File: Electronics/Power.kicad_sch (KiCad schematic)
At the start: 53 parts, among them IC1 TPS65251-1RHAR

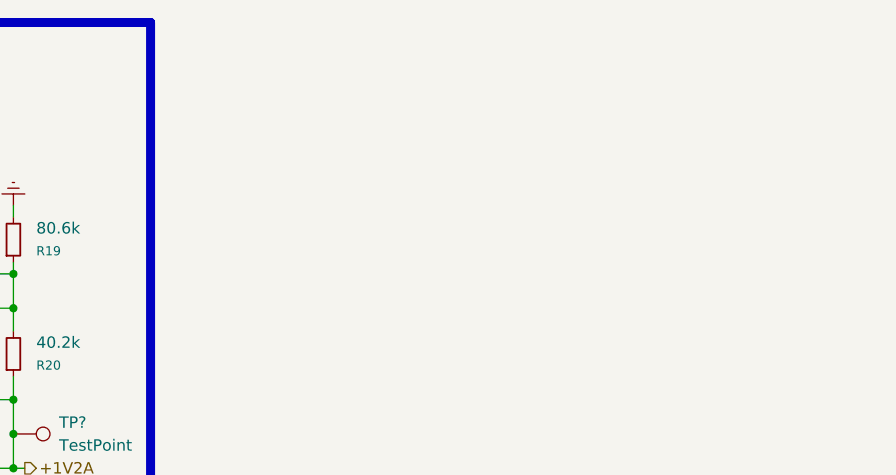
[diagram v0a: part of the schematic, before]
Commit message: RP2040 Added, Files Structure Changed
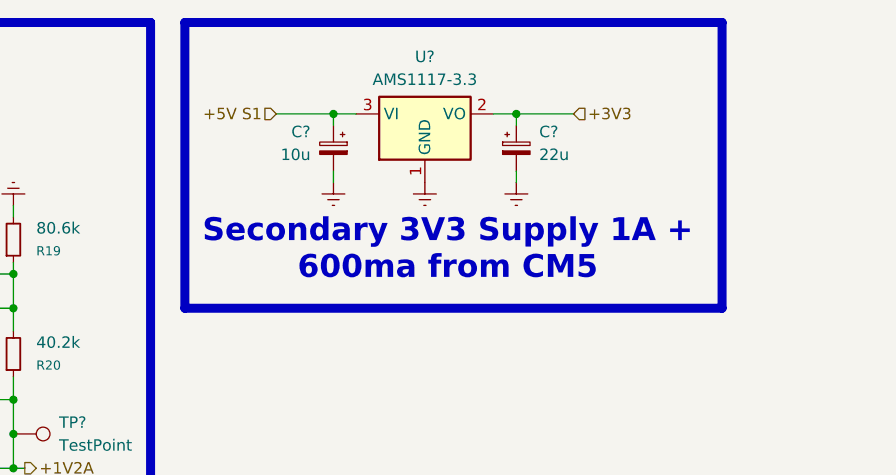
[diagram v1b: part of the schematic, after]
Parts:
- added C?: 10u, symbol Device:C_Polarized_Small
- added C?: 22u, symbol Device:C_Polarized_Small
- added U?: AMS1117-3.3, Package_TO_SOT_SMD:SOT-223-3_TabPin2, symbol Regulator_Linear:AMS1117-3.3
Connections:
- net +5V S1: now also C?.1, U?.3 (VI)
- new net +3V3: C?.1, U?.2 (VO)

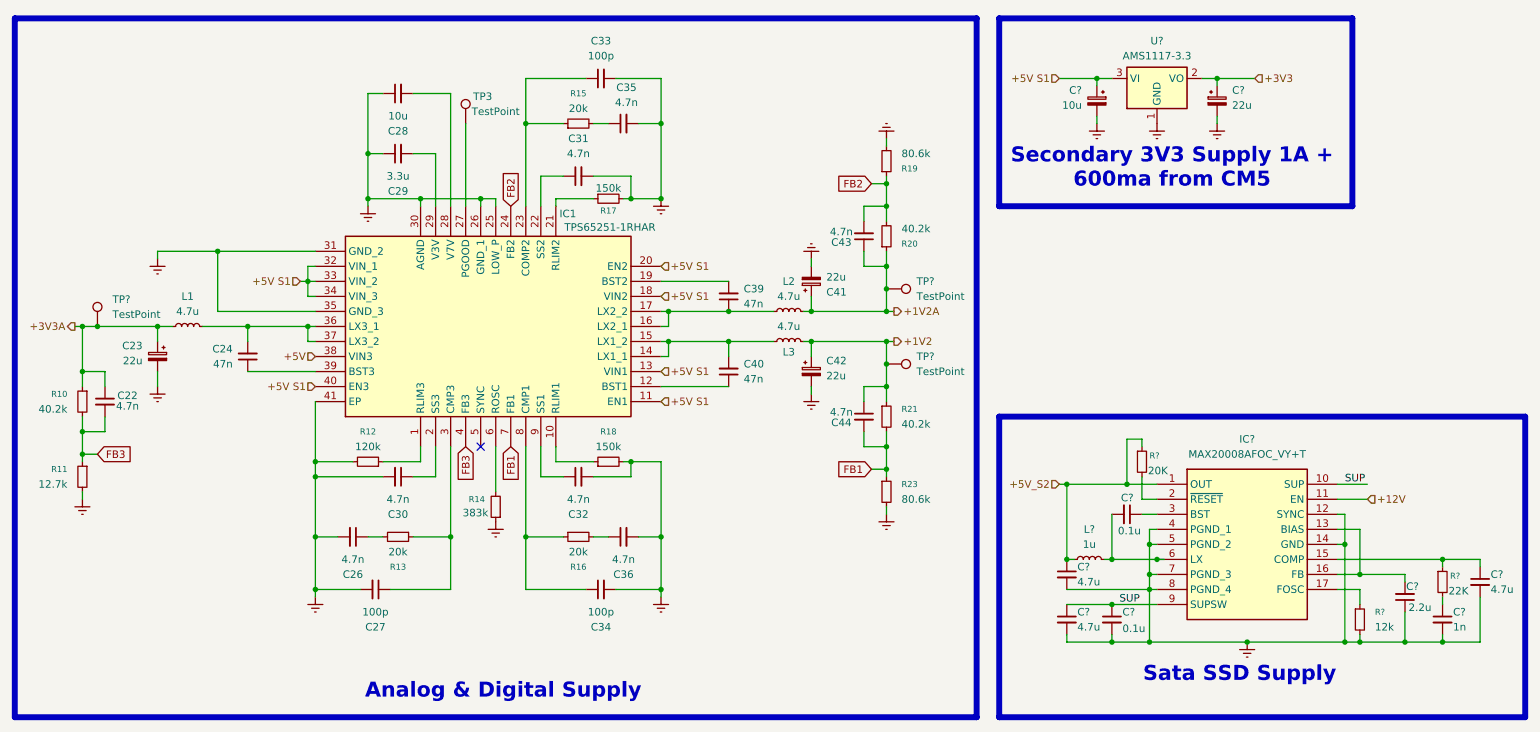
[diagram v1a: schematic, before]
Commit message: Starting the Sheet connections
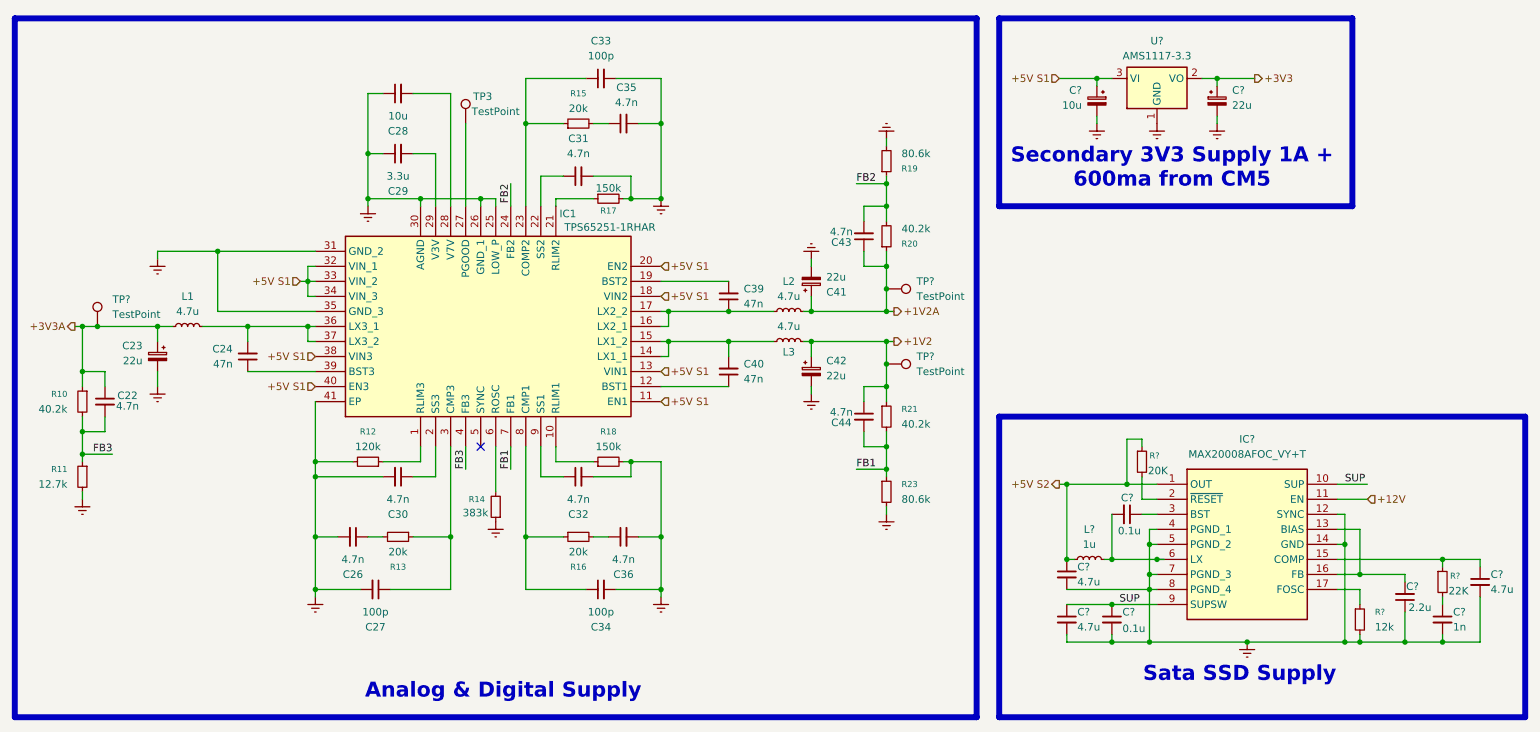
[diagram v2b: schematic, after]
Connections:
- net +5V is gone; now on net +5V S1: IC1.38 (VIN3)
- net +5V_S2 renamed +5V S2
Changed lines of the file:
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@@
 	(wire
 		(pts
-			(xy 162.56 44.45) (xy 165.1 44.45)
+			(xy 160.02 44.45) (xy 165.1 44.45)
 		)
 		(stroke
@@
 	(wire
 		(pts
-			(xy 162.56 92.71) (xy 165.1 92.71)
+			(xy 160.02 92.71) (xy 165.1 92.71)
 		)
 		(stroke
@@
 	(wire
 		(pts
+			(xy 101.6 44.45) (xy 101.6 48.26)
+		)
+		(stroke
+			(width 0)
+			(type default)
+		)
+	)
+	(wire
+		(pts
 			(xy 210.82 95.25) (xy 205.74 95.25)
 		)
@@
 	(wire
 		(pts
+			(xy 101.6 92.71) (xy 101.6 88.9)
+		)
+		(stroke
+			(width 0)
+			(type default)
+		)
+	)
+	(wire
+		(pts
 			(xy 161.29 88.9) (xy 165.1 88.9)
 		)
@@
 	(wire
 		(pts
+			(xy 93.98 92.71) (xy 93.98 88.9)
+		)
+		(stroke
+			(width 0)
+			(type default)
+		)
+	)
+	(wire
+		(pts
 			(xy 161.29 48.26) (xy 165.1 48.26)
 		)
@@
 	(wire
 		(pts
-			(xy 31.75 90.17) (xy 29.21 90.17)
+			(xy 34.29 90.17) (xy 29.21 90.17)
 		)
 		(stroke
@@
 		)
 	)
+	(label "FB2"
+		(at 160.02 44.45 0)
+		(effects
+			(font
+				(size 1.27 1.27)
+			)
+			(justify left bottom)
+		)
+	)
+	(label "FB2"
+		(at 101.6 44.45 270)
+		(effects
+			(font
+				(size 1.27 1.27)
+			)
+			(justify right bottom)
+		)
+	)
+	(label "FB1"
+		(at 160.02 92.71 0)
+		(effects
+			(font
+				(size 1.27 1.27)
+			)
+			(justify left bottom)
+		)
+	)
+	(label "FB3"
+		(at 34.29 90.17 180)
+		(effects
+			(font
+				(size 1.27 1.27)
+			)
+			(justify right bottom)
+		)
+	)
+	(label "FB3"
+		(at 93.98 92.71 90)
+		(effects
+			(font
+				(size 1.27 1.27)
+			)
+			(justify left bottom)
+		)
+	)
+	(label "FB1"
+		(at 101.6 92.71 90)
+		(effects
+			(font
+				(size 1.27 1.27)
+			)
+			(justify left bottom)
+		)
+	)
 	(label "SUP"
 		(at 242.57 95.25 0)
@@
 			)
 			(justify left bottom)
-		)
-	)
-	(global_label "FB3"
-		(shape input)
-		(at 31.75 90.17 0)
-		(fields_autoplaced yes)
-		(effects
-			(font
-				(size 1.27 1.27)
-			)
-			(justify left)
-		)
-		(property "Intersheetrefs" "${INTERSHEET_REFS}"
-			(at 38.3033 90.17 0)
-			(effects
-				(font
-					(size 1.27 1.27)
-				)
-				(justify left)
-				(hide yes)
-			)
-		)
-	)
-	(global_label "FB2"
-		(shape input)
-		(at 162.56 44.45 180)
-		(fields_autoplaced yes)
-		(effects
-			(font
-				(size 1.27 1.27)
-			)
-			(justify right)
-		)
-		(property "Intersheetrefs" "${INTERSHEET_REFS}"
-			(at 156.0067 44.45 0)
-			(effects
-				(font
-					(size 1.27 1.27)
-				)
-				(justify right)
-				(hide yes)
-			)
-		)
-	)
-	(global_label "FB1"
-		(shape input)
-		(at 162.56 92.71 180)
-		(fields_autoplaced yes)
-		(effects
-			(font
-				(size 1.27 1.27)
-			)
-			(justify right)
-		)
-		(property "Intersheetrefs" "${INTERSHEET_REFS}"
-			(at 156.0067 92.71 0)
-			(effects
-				(font
-					(size 1.27 1.27)
-				)
-				(justify right)
-				(hide yes)
-			)
-		)
-	)
-	(global_label "FB1"
-		(shape input)
-		(at 101.6 88.9 270)
-		(fields_autoplaced yes)
-		(effects
-			(font
-				(size 1.27 1.27)
-			)
-			(justify right)
-		)
-		(property "Intersheetrefs" "${INTERSHEET_REFS}"
-			(at 101.6 95.4533 90)
-			(effects
-				(font
-					(size 1.27 1.27)
-				)
-				(justify right)
-				(hide yes)
-			)
-		)
-	)
-	(global_label "FB3"
-		(shape input)
-		(at 93.98 88.9 270)
-		(fields_autoplaced yes)
-		(effects
-			(font
-				(size 1.27 1.27)
-			)
-			(justify right)
-		)
-		(property "Intersheetrefs" "${INTERSHEET_REFS}"
-			(at 93.98 95.4533 90)
-			(effects
-				(font
-					(size 1.27 1.27)
-				)
-				(justify right)
-				(hide yes)
-			)
-		)
-	)
-	(global_label "FB2"
-		(shape input)
-		(at 101.6 48.26 90)
-		(fields_autoplaced yes)
-		(effects
-			(font
-				(size 1.27 1.27)
-			)
-			(justify left)
-		)
-		(property "Intersheetrefs" "${INTERSHEET_REFS}"
-			(at 101.6 41.7067 90)
-			(effects
-				(font
-					(size 1.27 1.27)
-				)
-				(justify left)
-				(hide yes)
-			)
 		)
 	)
@@
 		)
 	)
-	(hierarchical_label "+5V_S2"
-		(shape input)
+	(hierarchical_label "+5V S2"
+		(shape output)
 		(at 194.31 95.25 180)
 		(effects
@@
 	)
 	(hierarchical_label "+3V3"
-		(shape input)
+		(shape output)
 		(at 227.33 26.67 0)
 		(effects
@@
 		)
 	)
-	(hierarchical_label "+5V"
+	(hierarchical_label "+5V S1"
 		(shape input)
 		(at 68.58 73.66 180)

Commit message: Footprints Selected
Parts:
- added C46: 100u, EEE_FTH101XAP:CAP_EEEFTH101XAP, symbol Device:C_Polarized_Small
- added C48: 0.1u, Capacitor_SMD:C_0603_1608Metric, symbol Device:C_Small
- added C50: 4.7u, Capacitor_SMD:C_0603_1608Metric, symbol Device:C_Small
- added D10, D11, D7, D8, D9: LED Green, LED_SMD:LED_0603_1608Metric, symbol Device:LED
- added R26, R27, R28, R29, R30: 1K, Resistor_SMD:R_0603_1608Metric, symbol Device:R_Small
- C20: renamed from C22; footprint (none) -> Capacitor_SMD:C_0603_1608Metric
- C21: renamed from C23; footprint (none) -> EEEFK1A220AR:CAP_EEEFK1A220AR
- C22: renamed from C24; footprint (none) -> Capacitor_SMD:C_0603_1608Metric
- C23: renamed from C26; footprint (none) -> Capacitor_SMD:C_0603_1608Metric
- C24: renamed from C27; footprint (none) -> Capacitor_SMD:C_0603_1608Metric
- C25: renamed from C28; footprint (none) -> Capacitor_SMD:C_0603_1608Metric
- C26: renamed from C29; footprint (none) -> Capacitor_SMD:C_0603_1608Metric
- C27: renamed from C30; footprint (none) -> Capacitor_SMD:C_0603_1608Metric
- C28: renamed from C31; footprint (none) -> Capacitor_SMD:C_0603_1608Metric
- C29: renamed from C32; footprint (none) -> Capacitor_SMD:C_0603_1608Metric
- C30: renamed from C33; footprint (none) -> Capacitor_SMD:C_0603_1608Metric
- C31: renamed from C34; footprint (none) -> Capacitor_SMD:C_0603_1608Metric
- C32: renamed from C35; footprint (none) -> Capacitor_SMD:C_0603_1608Metric
- C33: renamed from C36; footprint (none) -> Capacitor_SMD:C_0603_1608Metric
- C34: renamed from C39; footprint (none) -> Capacitor_SMD:C_0603_1608Metric
- C35: renamed from C40; footprint (none) -> Capacitor_SMD:C_0603_1608Metric
- C36: renamed from C41; footprint (none) -> EEEFK1A220AR:CAP_EEEFK1A220AR
- C37: renamed from C42; footprint (none) -> EEEFK1A220AR:CAP_EEEFK1A220AR
- C38: renamed from C43; footprint (none) -> Capacitor_SMD:C_0603_1608Metric
- C39: renamed from C44; footprint (none) -> Capacitor_SMD:C_0603_1608Metric
- C40, C41, C43, C44, C47, C49, C51: renamed from C?; footprint (none) -> Capacitor_SMD:C_0603_1608Metric
- C42: renamed from C?; footprint (none) -> EEEFK1H100UR:CAP_EEEFK1H100UR
- C45: renamed from C?; footprint (none) -> EEEFK1A220AR:CAP_EEEFK1A220AR
- IC1: footprint QFN50P600X600X100-41N-D -> TPS65251-1RHAR:QFN50P600X600X100-41N-D
- IC2: renamed from IC?; footprint MAX20008AFOCVYT -> MAX20008AFOC_VY+T:MAX20008AFOCVYT
- L1, L2, L3: footprint (none) -> SRN5040-4R7M:INDPM5050X400N
- L4: renamed from L?; footprint (none) -> SRN5040TA-1R0M:SRN5040TA1R0M
- R13: renamed from R10; footprint (none) -> Resistor_SMD:R_0603_1608Metric
- R14: renamed from R11; footprint (none) -> Resistor_SMD:R_0603_1608Metric
- R15: renamed from R12; footprint (none) -> Resistor_SMD:R_0603_1608Metric
- R16: renamed from R13; footprint (none) -> Resistor_SMD:R_0603_1608Metric
- R17: renamed from R14; footprint (none) -> Resistor_SMD:R_0603_1608Metric
- R18: renamed from R15; footprint (none) -> Resistor_SMD:R_0603_1608Metric
- R19: renamed from R16; footprint (none) -> Resistor_SMD:R_0603_1608Metric
- R20: renamed from R17; footprint (none) -> Resistor_SMD:R_0603_1608Metric
- R21: renamed from R18; footprint (none) -> Resistor_SMD:R_0603_1608Metric
- R22: renamed from R19; footprint (none) -> Resistor_SMD:R_0603_1608Metric
- R23: renamed from R20; footprint (none) -> Resistor_SMD:R_0603_1608Metric
- R24: renamed from R21; footprint (none) -> Resistor_SMD:R_0603_1608Metric
- R25: renamed from R23; footprint (none) -> Resistor_SMD:R_0603_1608Metric
- R31, R32, R33: renamed from R?; footprint (none) -> Resistor_SMD:R_0603_1608Metric
- TP6, TP8, TP9: renamed from TP?; footprint (none) -> TestPoint:TestPoint_Pad_1.0x1.0mm
- TP7: renamed from TP3; footprint (none) -> TestPoint:TestPoint_Pad_1.0x1.0mm
- gave numbers to parts that had none: 1
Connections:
- net +12V: now also C46.1, C48.1, C50.1
- net +1V2: now also R27.2
- net +1V2A: now also R26.2
- net +3V3: now also R28.2
- net +3V3A: now also R29.2
- net +5V S2: now also R30.2
- new net: D10.1 (K), D11.1 (K), D7.1 (K), D8.1 (K), D9.1 (K)
- new net: D8.2 (A), R27.1
- new net: D7.2 (A), R26.1
- new net: D10.2 (A), R29.1
- new net: D9.2 (A), R28.1
- new net: C46.2, C48.2, C50.2
- new net: D11.2 (A), R30.1

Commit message: Footprints selected, Hiracicle connections created, Pcb next
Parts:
- removed D7, D8: LED Green, LED_SMD:LED_0603_1608Metric, symbol Device:LED
- removed R26, R27: 1K, Resistor_SMD:R_0603_1608Metric, symbol Device:R_Small
- added TP11, TP6: TestPoint, TestPoint:TestPoint_Pad_1.0x1.0mm, symbol Connector:TestPoint
- C20: renamed from C30; footprint Capacitor_SMD:C_0603_1608Metric -> Capacitor_SMD:C_0402_1005Metric
- C21: renamed from C25; footprint Capacitor_SMD:C_0603_1608Metric -> Capacitor_SMD:C_0805_2012Metric
- C24: renamed from C32; value 4.7n -> 4n7; footprint Capacitor_SMD:C_0603_1608Metric -> Capacitor_SMD:C_0402_1005Metric
- C25: renamed from C26; value 3.3u -> 3u3; footprint Capacitor_SMD:C_0603_1608Metric -> Capacitor_SMD:C_0805_2012Metric
- C26: renamed from C28; value 4.7n -> 4n7; footprint Capacitor_SMD:C_0603_1608Metric -> Capacitor_SMD:C_0402_1005Metric
- C27: renamed from C38; value 4.7n -> 4n7; footprint Capacitor_SMD:C_0603_1608Metric -> Capacitor_SMD:C_0402_1005Metric
- C29: renamed from C34; footprint Capacitor_SMD:C_0603_1608Metric -> Capacitor_SMD:C_0402_1005Metric
- C31: renamed from C22; footprint Capacitor_SMD:C_0603_1608Metric -> Capacitor_SMD:C_0402_1005Metric
- C32: renamed from C35; footprint Capacitor_SMD:C_0603_1608Metric -> Capacitor_SMD:C_0402_1005Metric
- C34: renamed from C20; value 4.7n -> 4n7; footprint Capacitor_SMD:C_0603_1608Metric -> Capacitor_SMD:C_0402_1005Metric
- C35: renamed from C39; value 4.7n -> 4n7; footprint Capacitor_SMD:C_0603_1608Metric -> Capacitor_SMD:C_0402_1005Metric
- C36: renamed from C27; value 4.7n -> 4n7; footprint Capacitor_SMD:C_0603_1608Metric -> Capacitor_SMD:C_0402_1005Metric
- C37: renamed from C29; value 4.7n -> 4n7; footprint Capacitor_SMD:C_0603_1608Metric -> Capacitor_SMD:C_0402_1005Metric
- C38: renamed from C44; value 0.1u -> 100n
- C40: renamed from C48; value 0.1u -> 100n; footprint Capacitor_SMD:C_0603_1608Metric -> Capacitor_SMD:C_0402_1005Metric
- C41: renamed from C50; value 4.7u -> 4u7; footprint Capacitor_SMD:C_0603_1608Metric -> Capacitor_SMD:C_0805_2012Metric
- C42: renamed from C23; value 4.7n -> 4n7; footprint Capacitor_SMD:C_0603_1608Metric -> Capacitor_SMD:C_0402_1005Metric
- C43: renamed from C33; value 4.7n -> 4n7; footprint Capacitor_SMD:C_0603_1608Metric -> Capacitor_SMD:C_0402_1005Metric
- C44: renamed from C40; value 4.7u -> 4u7; footprint Capacitor_SMD:C_0603_1608Metric -> Capacitor_SMD:C_0805_2012Metric
- C45: renamed from C51; value 4.7u -> 4u7; footprint Capacitor_SMD:C_0603_1608Metric -> Capacitor_SMD:C_0805_2012Metric
- C46: renamed from C24; footprint Capacitor_SMD:C_0603_1608Metric -> Capacitor_SMD:C_0402_1005Metric
- C47: renamed from C31; footprint Capacitor_SMD:C_0603_1608Metric -> Capacitor_SMD:C_0402_1005Metric
- C48: renamed from C47; value 2.2u -> 2u2
- C49: renamed from C41; value 4.7u -> 4u7; footprint Capacitor_SMD:C_0603_1608Metric -> Capacitor_SMD:C_0805_2012Metric
- C50: renamed from C43; value 0.1u -> 100n
- C51: renamed from C49; footprint Capacitor_SMD:C_0603_1608Metric -> Capacitor_SMD:C_0402_1005Metric
- L1: renamed from L2; value 4.7u -> 4u7
- L2: renamed from L1; value 4.7u -> 4u7
- L3: value 4.7u -> 4u7
- R14: renamed from R22; value 80.6k -> 80K6
- R16: renamed from R23; value 40.2k -> 40K2
- R17: renamed from R28; value 1K -> 270
- R18: renamed from R29; value 1K -> 270
- R20: renamed from R13; value 40.2k -> 40K2
- R21: renamed from R24; value 40.2k -> 40K2
- R25: renamed from R14; value 12.7k -> 12K7
- R26: renamed from R25; value 80.6k -> 80K6
- TP10: renamed from TP9; now not fitted; now left out of the parts list
- TP8: now not fitted; now left out of the parts list
- TP9: renamed from TP6; now not fitted; now left out of the parts list
- renumbered C42 to C22, C45 to C23, C36 to C28, C21 to C30, C37 to C33, C46 to C39, D9 to D7, D10 to D8, D11 to D9, R18 to R13, R20 to R15, R30 to R19, R15 to R22, R21 to R23, R31 to R24, R17 to R27, R16 to R28, R19 to R29, R33 to R30, R32 to R31
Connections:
- net +3V3: now also TP6.1
- net +5V S2: now also TP11.1
- net gnd: now reaches D7.1 (K), D8.1 (K), D9.1 (K)
- net gnd: now also C20.2, C21.1, C22.2, C23.2, C24.2, C25.1, C26.2, C28.2, C30.2, C33.2, C36.2, C37.2, C39.2, C40.2, C41.2, C42.2, C43.2, C44.2, C45.2, C46.2, C47.2, C48.1, C49.2, C50.2, C51.2, IC1.25 (LOW_P), IC1.26 (GND_1), IC1.30 (AGND), IC1.31 (GND_2), IC1.35 (GND_3), IC1.41 (EP), IC2.12 (SYNC), IC2.14 (GND), IC2.4 (PGND_1), IC2.5 (PGND_2), IC2.7 (PGND_3), IC2.8 (PGND_4), R14.2, R15.2, R22.2, R23.2, R25.2, R26.2, R27.1, R31.2, U6.1 (GND)
